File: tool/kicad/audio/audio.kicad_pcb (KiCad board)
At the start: 2 copper layers, 115 x 45 mm, 146 parts, among them J1 MICRO-USB-AB, K1 CONN_3, K2 CONN_3, P1 TEST_POINT, P10 TEST_POINT, P11 TEST_POINT, P12 TEST_POINT, P13 TEST_POINT, P14 TEST_POINT, P15 TEST_POINT, P16 TEST_POINT, P17 TEST_POINT, P18 TEST_POINT, P19 TEST_POINT, P2 TEST_POINT, P20 TEST_POINT, P21 TEST_POINT, P22 TEST_POINT, P23 TEST_POINT, P24 TEST_POINT, P25 TEST_POINT, P26 TEST_POINT, P27 TEST_POINT, P28 TEST_POINT, P29 TEST_POINT, P3 TEST_POINT, P30 CONN_3X2, P31 CONN_2, P32 CONN_2, P33 TEST_POINT, P34 TEST_POINT, P35 CONN_6, P37 TEST_POINT, P38 TEST_POINT, P4 TEST_POINT, P5 MIDI-IN, P6 TEST_POINT, P7 TEST_POINT, P8 TEST_POINT, P9 TEST_POINT, U1 SN74LVC2T45, U2 ST-USBLC6-2, U3 EFM32GG332, U4 YM2413, U5 LM386, U6 LM386, U7 ACPL-M21L, X1 48Mhz, X2 CRYSTAL

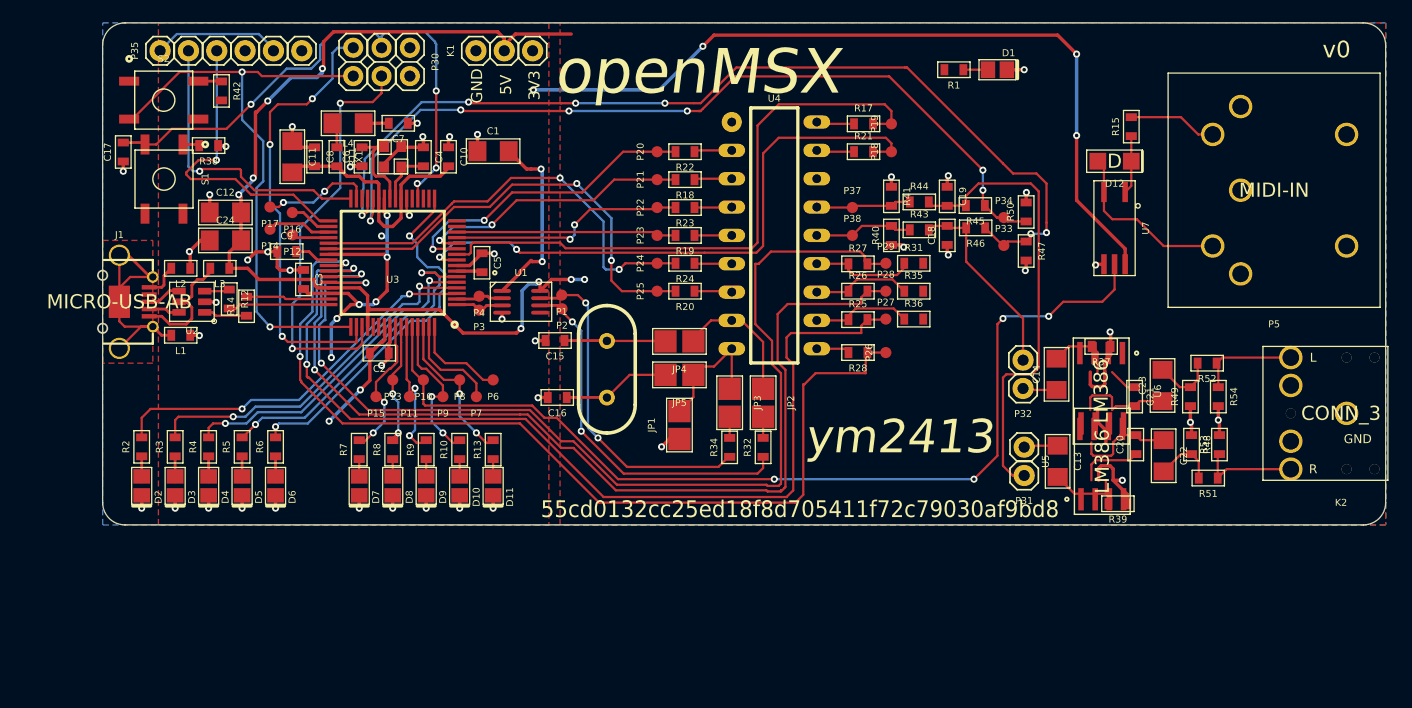
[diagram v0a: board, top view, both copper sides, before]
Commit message: fix and layout audio/midi board
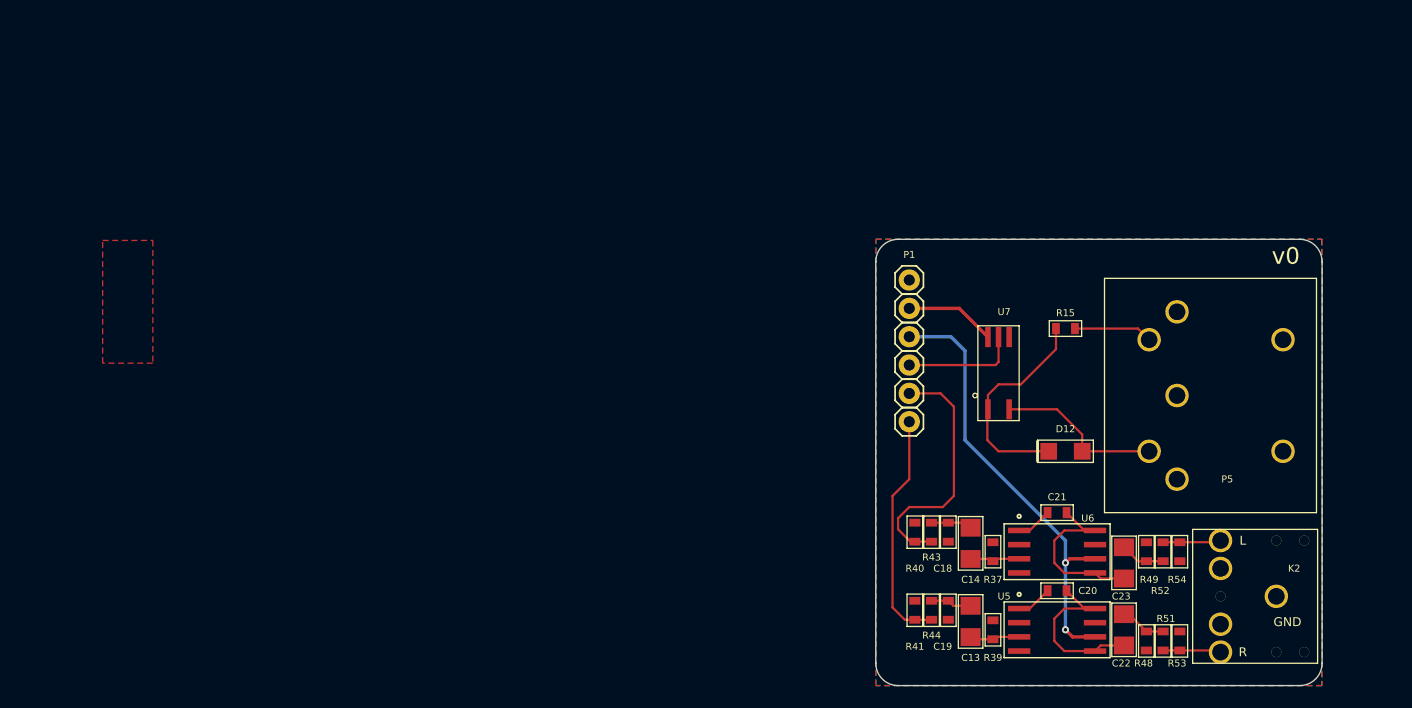
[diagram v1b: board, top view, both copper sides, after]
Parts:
- removed C1, C11: 10uF, pretty:1206
- removed C10, C8: 10nF, pretty:0603_S
- removed C12, C24: 4.7uF, pretty:1206
- removed C15, C16: 20pF/NC, pretty:0603_S
- removed C17, C2, C3, C5: 100nF, pretty:0603_S
- removed C4, C6: 18pF, pretty:0603_S
- removed C7, C9: 1uF, pretty:0603_S
- removed D1, D10, D11, D2, D3, D4, D5, D6, D7, D8, D9: LED, pretty:0805_LED
- removed J1: MICRO-USB-AB, pretty:USB-MICRO-AB-Molex-47590-0001
- removed JP1, JP2, JP3, JP4, JP5: SJ, pretty:Solder_Jumper_2mm
- removed K1: CONN_3, pretty:PIN_1X3
- removed L1, L2, L3: FB, pretty:0603_S
- removed L4: L, pretty:1206
- removed P10, P11, P12, P13, P14, P15, P16, P17, P18, P19, P2, P20, P21, P22, P23, P24, P25, P26, P27, P28, P29, P3, P33, P34, P37, P38, P4, P6, P7, P8, P9: TEST_POINT, pretty:Test_Pad_1mm
- removed P30: CONN_3X2, pretty:PIN_2X3_ALT_S
- removed P31, P32: CONN_2, pretty:PIN_1X2_S
- removed P35: CONN_6, pretty:PIN_1X6_S
- removed R1, R10, R13, R2, R3, R4, R5, R6, R7, R8, R9: 3k3, pretty:0603_S
- removed R11: 1, pretty:0603_S
- removed R12, R14: 15, pretty:0603_S
- removed R17, R18, R19, R20, R21, R22, R23, R24, R25, R26, R27, R28, R32, R34: 22, pretty:0603_S
- removed R31, R35: 100k, pretty:0603_S
- removed R36: 100k/NC, pretty:0603_S
- removed R38, R42: 100, pretty:0603_S
- removed R45, R46, R47, R50: 2k2, pretty:0603_S
- removed S1, S2: TACTSW, pretty:BUTTON_ALPS_SMD_5.2mm_SKQG_S
- removed U1: SN74LVC2T45, pretty:R-PDSO-G8
- removed U2: ST-USBLC6-2, pretty:SOT-23-6L
- removed U3: EFM32GG332, pretty:TQFP64
- removed U4: YM2413, pretty:DIL18
- removed X1: 48Mhz, pretty:CRYSTAL-TXC-8Z-2.5x2
- removed X2: CRYSTAL, HC-49V
- P1: value TEST_POINT -> CONN_6; footprint pretty:Test_Pad_1mm -> pretty:PIN_1X6_S
- moved R41 37.2 mm to (78.5, 58.2)
- moved C19 37.1 mm to (81.5, 58.2), turned to 90 degrees
- moved R44 36.6 mm to (80.0, 58.2), turned to 90 degrees
- moved P1 31.5 mm to (78.0, 35.0), turned to 0 degrees
- moved R43 27.1 mm to (80.0, 51.2), turned to 90 degrees
- moved R40 26.7 mm to (78.5, 51.2), turned to 270 degrees
- moved C18 26.6 mm to (81.5, 51.2)
- moved D12 26.4 mm to (92.0, 44.0), turned to 0 degrees
- moved R37 20.8 mm to (85.5, 53.0), turned to 270 degrees
- moved P5 19.3 mm to (105.0, 39.0)
- moved R15 19.0 mm to (92.0, 33.0), turned to 0 degrees
- moved R48 18.1 mm to (99.2, 61.0), turned to 90 degrees
- moved R53 18.0 mm to (102.2, 61.0)
- moved K2 17.6 mm to (110.4, 57.0)
- moved R52 17.4 mm to (100.8, 53.0), turned to 270 degrees
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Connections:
- C13 pad 1: Net-(C13-Pad1) -> /ROI
- C14 pad 1: Net-(C14-Pad1) -> /MOI
- P1 pad 1: /XOUT -> GND
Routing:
- net +3.3V: track 133.4 -> 8.12 mm, vias 15 -> 0
- net /~IC: track 94.0 -> 0.00 mm, vias 2 -> 0
- net /~CS: track 89.1 -> 0.00 mm, vias 2 -> 0
- net /~WE: track 87.9 -> 0.00 mm, vias 2 -> 0
- net /MOd2: track 87.0 -> 0.00 mm, vias 6 -> 0
- net /A0: track 85.0 -> 0.00 mm, vias 2 -> 0
- net /MIDI_IN: track 88.4 -> 10.3 mm, vias 4 -> 0
- net GND: track 77.3 -> 0.00 mm, vias 44 -> 0
- net /ROd2: track 76.8 -> 0.00 mm, vias 6 -> 0
- net /D0: track 54.8 -> 0.00 mm, vias 2 -> 0
- net /D1: track 54.5 -> 0.00 mm
- net +5V: track 94.1 -> 40.0 mm, vias 8 -> 2
- net /SWC: track 53.6 -> 0.00 mm, vias 2 -> 0
- net /~RESET: track 50.7 -> 0.00 mm, vias 4 -> 0
- net /D7: track 40.8 -> 0.00 mm, vias 2 -> 0
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- added copper zone on F.Cu, net GND
- removed copper zone on F.Cu, net +3.3V
- removed copper zone on F.Cu, net +5V
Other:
- board size 115 x 45 mm -> 40 x 40 mm
- board text removed: "3V3"
- board text removed: "55cd0132cc25ed18f8d705411f72c79030af9bd8"
- board text removed: "5V"
- board text removed: "GND"
- board text removed: "openMSX"
- board text removed: "ym2413"

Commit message: add silk to bottom to please oshpark
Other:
- board text added: "openMSX"
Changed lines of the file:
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@@
     (links 53)
     (no_connects 0)
-    (area 5.7 24.949999 117.602401 65.6399)
+    (area 5.7 24.949999 117.602401 65.050001)
     (thickness 1.6)
-    (drawings 9)
+    (drawings 10)
     (tracks 95)
     (zones 0)
@@
       (net 11 /RO))
   )
+  (gr_text openMSX (at 90 30) (layer B.SilkS)
+    (effects (font (size 1.5 1.5) (thickness 0.3)) (justify mirror))
+  )
   (gr_line (start 75 27) (end 75 63) (angle 90) (layer Edge.Cuts) (width 0.1))

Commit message: store
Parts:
- R40, R41: value 2k2 -> 2k2/NC
- R43, R44: value 4k7/NC -> 4k7/0
